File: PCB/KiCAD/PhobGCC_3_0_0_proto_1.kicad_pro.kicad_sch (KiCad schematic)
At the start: 110 parts, among them J1 Conn_01x06_Female, J11 Conn_01x02, J14 Conn_01x06, J15 Conn_01x06, J2 Conn_01x02, J3 Conn_01x02, J4 Conn_01x01, J5 Rumble, J6 Conn_01x06, J8 USB_B_Micro, Q1 Q_NMOS_GSD, Q2 Q_PMOS_GDS, Q3 Q_NMOS_GSD, SW1 A, SW10 Dup, SW11 Dright, SW12 Ddown, SW2 B, SW3 X, SW4 Y, SW5 Start, SW6 L, SW7 R, SW8 Z, SW9 Dleft, U1 MCP3202, U10 DRV5055A3xDBZxQ1, U11 DRV5055A3xDBZxQ1, U12 USBLC6-2P6, U13 USBLC6-2P6, U2 Stickbox_Assembly_Main, U3 MCP3202, U4 DRV5055A3xDBZxQ1, U5 Stickbox_Assembly_CStick, U6 AMS1117-3.3, U7 W25Q128JVS, U8 RP2040, U9 DRV5055A3xDBZxQ1, Y1 Crystal_GND24

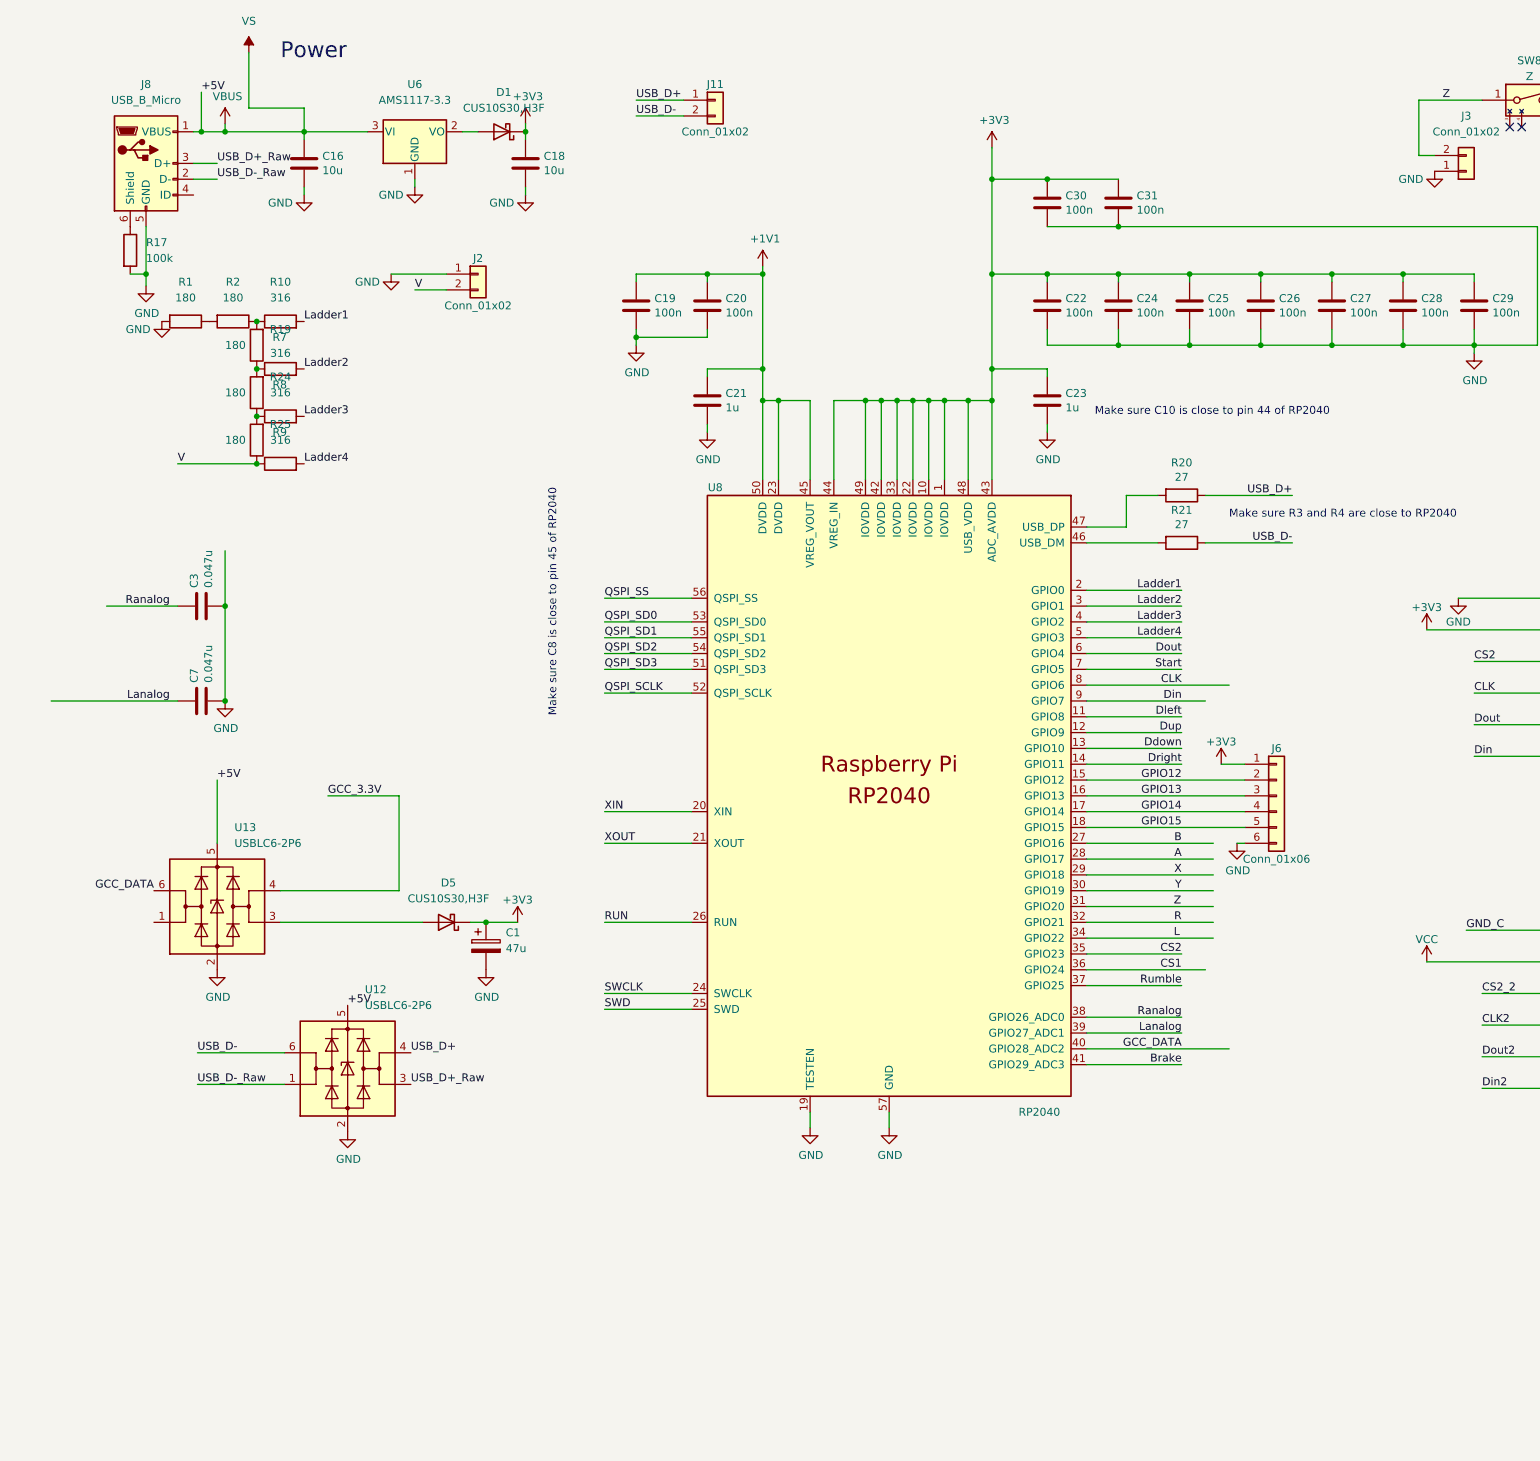
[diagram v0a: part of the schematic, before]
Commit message: RP2040 to RP2350 Conversion
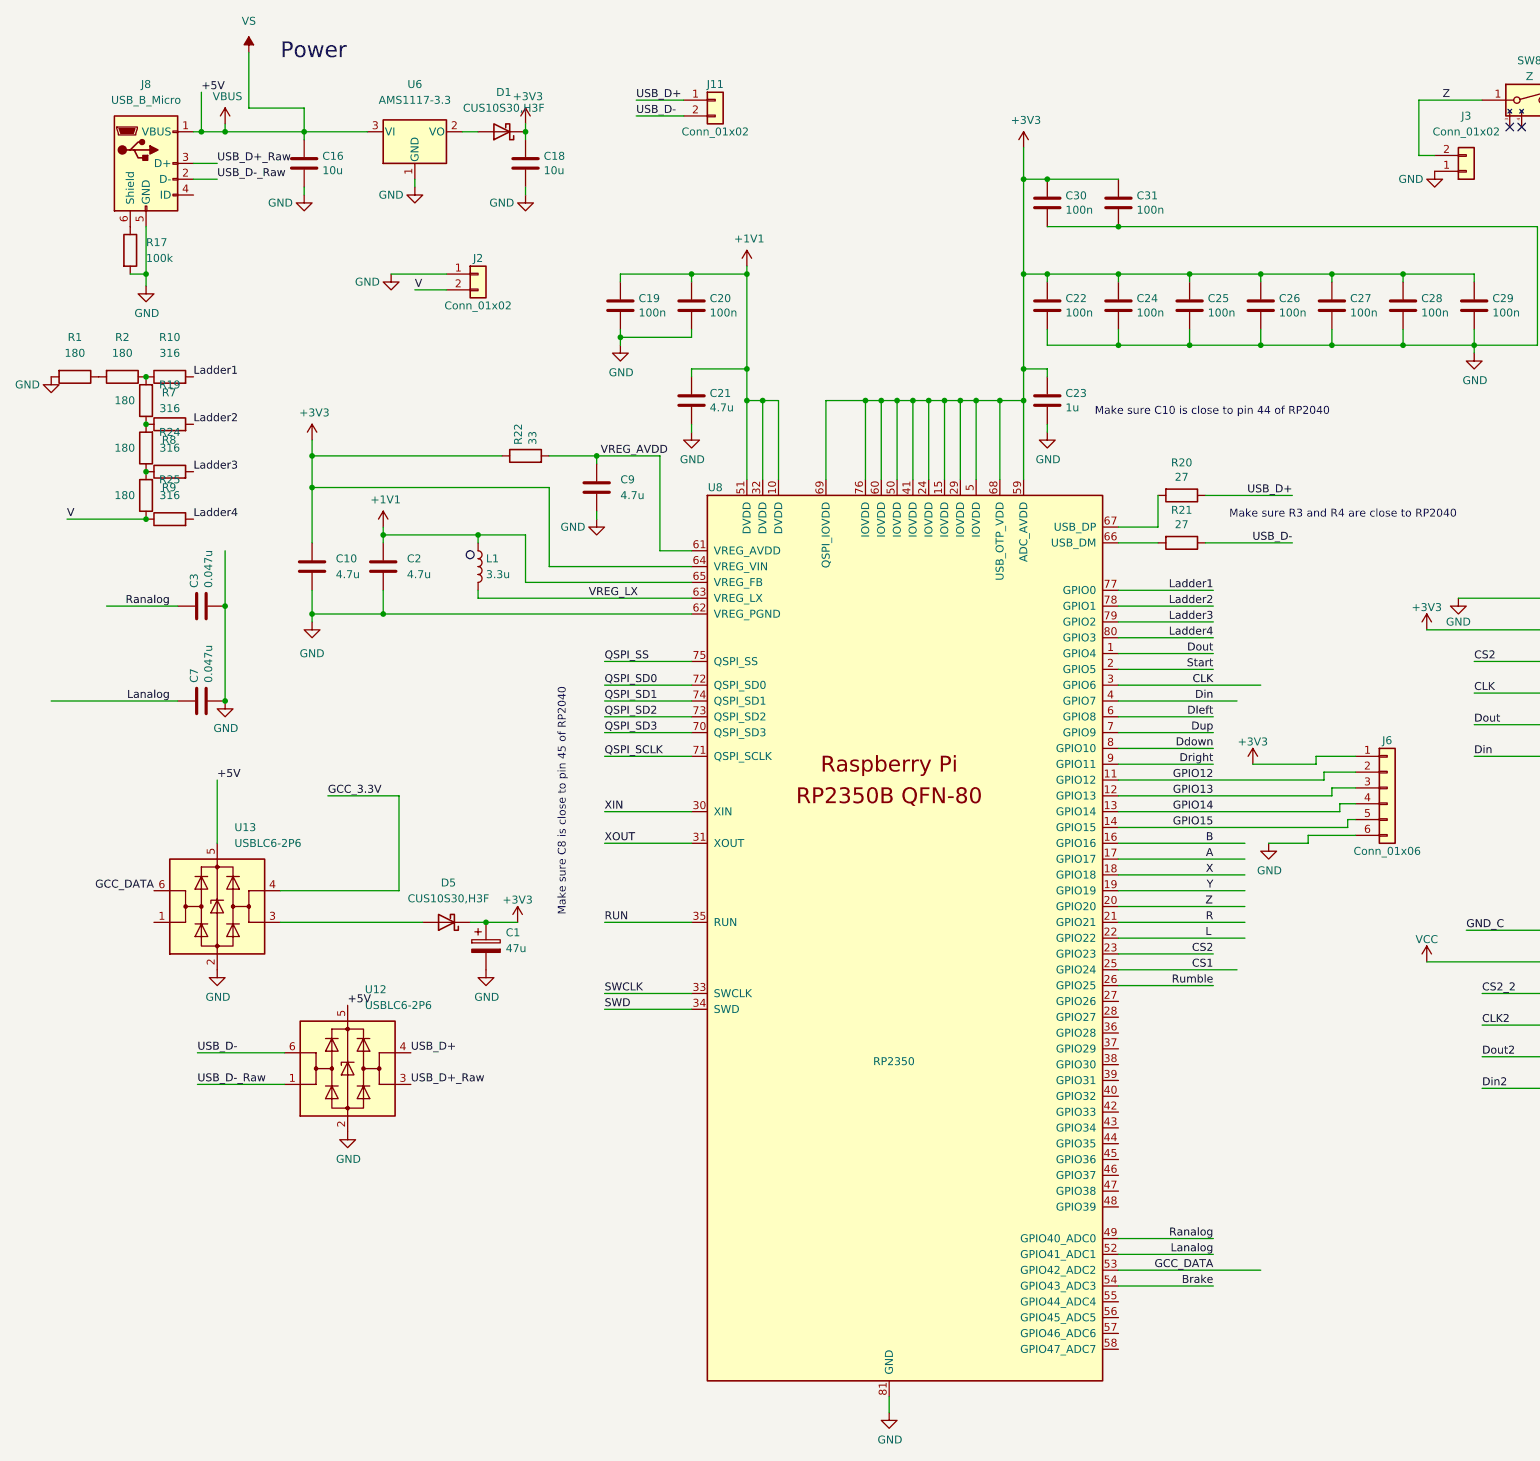
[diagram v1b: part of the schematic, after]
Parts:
- added C10, C2: 4.7u, RP2350_80QFN_minimal:C_0402_1005Metric_small_pads, symbol Device:C
- added C9: 4.7u, Capacitor_SMD:C_0402_1005Metric, symbol Device:C
- added L1: 3.3u, RP2350_80QFN_minimal:L_pol_2016, symbol Device:L
- added R22: 33, Resistor_SMD:R_0402_1005Metric, symbol Device:R
- C21: value 1u -> 4.7u
- U8: value RP2040 -> RP2350; footprint PhobGCC_2_0_0_footprints:RP2040-QFN-56 -> RP2350_80QFN_minimal:RP2350-QFN-80-1EP_10x10_P0.4mm_EP3.4x3.4mm_ThermalVias; symbol MCU_RaspberryPi_RP2040:RP2040 -> MCU_RaspberryPi_RP2350:RP2350_80QFN
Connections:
- net +1V1: now also U8.10 (DVDD), U8.32 (DVDD), U8.51 (DVDD), U8.65 (VREG_FB), C2.1, L1.1; no longer U8.23 (DVDD), U8.45 (VREG_VOUT), U8.50 (DVDD)
- net +3V3: now also U8.15 (IOVDD), U8.24 (IOVDD), U8.29 (IOVDD), U8.41 (IOVDD), U8.5 (IOVDD), U8.50 (IOVDD), U8.59 (ADC_AVDD), U8.60 (IOVDD), U8.64 (VREG_VIN), U8.68 (USB_OTP_VDD), U8.69 (QSPI_IOVDD), U8.76 (IOVDD), C10.1, R22.1; no longer U8.1 (IOVDD), U8.10 (IOVDD), U8.22 (IOVDD), U8.33 (IOVDD), U8.42 (IOVDD), U8.43 (ADC_AVDD), U8.44 (VREG_IN), U8.48 (USB_VDD), U8.49 (IOVDD)
- net A: now also U8.17 (GPIO17); no longer U8.28 (GPIO17)
- net B: now also U8.16 (GPIO16); no longer U8.27 (GPIO16)
- net Brake: now also U8.54 (GPIO43_ADC3); no longer U8.41 (GPIO29_ADC3)
- net CLK: now also U8.3 (GPIO6); no longer U8.8 (GPIO6)
- net CS1: now also U8.25 (GPIO24); no longer U8.36 (GPIO24)
- net CS2: now also U8.23 (GPIO23); no longer U8.35 (GPIO23)
- net Ddown: now also U8.8 (GPIO10); no longer U8.13 (GPIO10)
- net Din: now also U8.4 (GPIO7); no longer U8.9 (GPIO7)
- net Dleft: now also U8.6 (GPIO8); no longer U8.11 (GPIO8)
- net Dout: now also U8.1 (GPIO4); no longer U8.6 (GPIO4)
- net Dright: now also U8.9 (GPIO11); no longer U8.14 (GPIO11)
- net Dup: now also U8.7 (GPIO9); no longer U8.12 (GPIO9)
- net GCC_DATA: now also U8.53 (GPIO42_ADC2); no longer U8.40 (GPIO28_ADC2)
- net GND: now also U8.62 (VREG_PGND), U8.81 (GND), C10.2, C2.2, C9.2; no longer U8.19 (TESTEN), U8.57 (GND)
- net GPIO12: now also U8.11 (GPIO12); no longer U8.15 (GPIO12)
- net GPIO13: now also U8.12 (GPIO13); no longer U8.16 (GPIO13)
- net GPIO14: now also U8.13 (GPIO14); no longer U8.17 (GPIO14)
- net GPIO15: now also U8.14 (GPIO15); no longer U8.18 (GPIO15)
- net L: now also U8.22 (GPIO22); no longer U8.34 (GPIO22)
- net Ladder1: now also U8.77 (GPIO0); no longer U8.2 (GPIO0)
- net Ladder2: now also U8.78 (GPIO1); no longer U8.3 (GPIO1)
- net Ladder3: now also U8.79 (GPIO2); no longer U8.4 (GPIO2)
- net Ladder4: now also U8.80 (GPIO3); no longer U8.5 (GPIO3)
- net Lanalog: now also U8.52 (GPIO41_ADC1); no longer U8.39 (GPIO27_ADC1)
- net QSPI_SCLK: now also U8.71 (QSPI_SCLK); no longer U8.52 (QSPI_SCLK)
- net QSPI_SD0: now also U8.72 (QSPI_SD0); no longer U8.53 (QSPI_SD0)
- net QSPI_SD1: now also U8.74 (QSPI_SD1); no longer U8.55 (QSPI_SD1)
- net QSPI_SD2: now also U8.73 (QSPI_SD2); no longer U8.54 (QSPI_SD2)
- net QSPI_SD3: now also U8.70 (QSPI_SD3); no longer U8.51 (QSPI_SD3)
- net QSPI_SS: now also U8.75 (QSPI_SS); no longer U8.56 (QSPI_SS)
- net R: now also U8.21 (GPIO21); no longer U8.32 (GPIO21)
- net RUN: now also U8.35 (RUN); no longer U8.26 (RUN)
- net Ranalog: now also U8.49 (GPIO40_ADC0); no longer U8.38 (GPIO26_ADC0)
- net Rumble: now also U8.26 (GPIO25); no longer U8.37 (GPIO25)
- net SWCLK: now also U8.33 (SWCLK); no longer U8.24 (SWCLK)
- net SWD: now also U8.34 (SWD); no longer U8.25 (SWD)
- net Start: now also U8.2 (GPIO5); no longer U8.7 (GPIO5)
- net X: now also U8.18 (GPIO18); no longer U8.29 (GPIO18)
- net XIN: now also U8.30 (XIN); no longer U8.20 (XIN)
- net XOUT: now also U8.31 (XOUT); no longer U8.21 (XOUT)
- net Y: now also U8.19 (GPIO19); no longer U8.30 (GPIO19)
- net Z: now also U8.20 (GPIO20); no longer U8.31 (GPIO20)
- net at U8.46 (GPIO37): no longer R21.2
- net at U8.47 (GPIO38): no longer R20.2
- new net: R21.2, U8.66 (USB_DM)
- new net: R20.2, U8.67 (USB_DP)
- new net VREG_AVDD: C9.1, R22.2, U8.61 (VREG_AVDD)
- new net VREG_LX: L1.2, U8.63 (VREG_LX)
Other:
- moved on the sheet: C19, C20, C21, J6, R1, R10, R19, R2, R24, R25, R7, R8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
